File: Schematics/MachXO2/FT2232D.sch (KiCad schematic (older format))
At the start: 43 parts, among them J3 USB_B_Micro, U2 FT2232D, U4 93C56, X2 6.00MHz

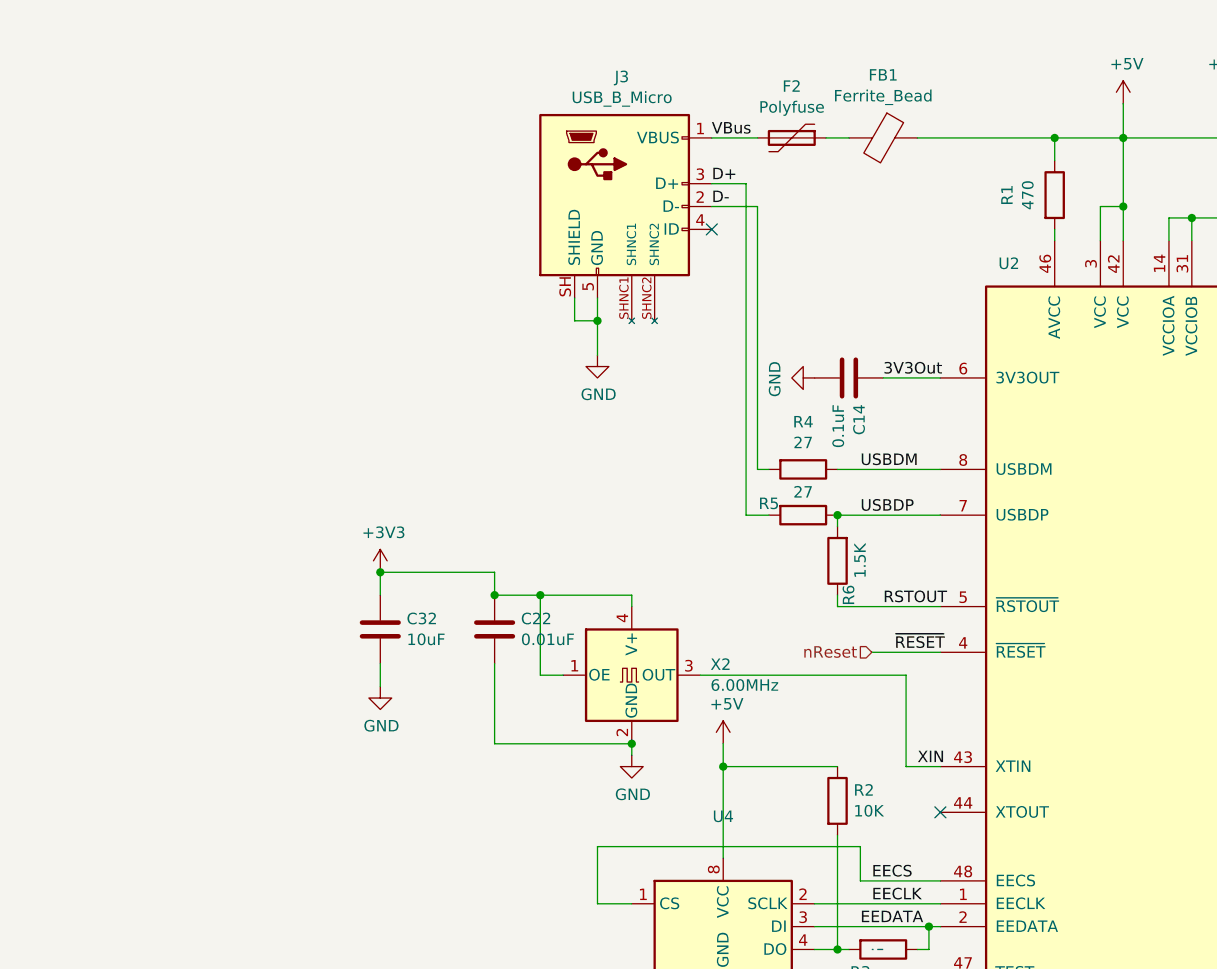
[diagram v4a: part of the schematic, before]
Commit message: asq bug fix.
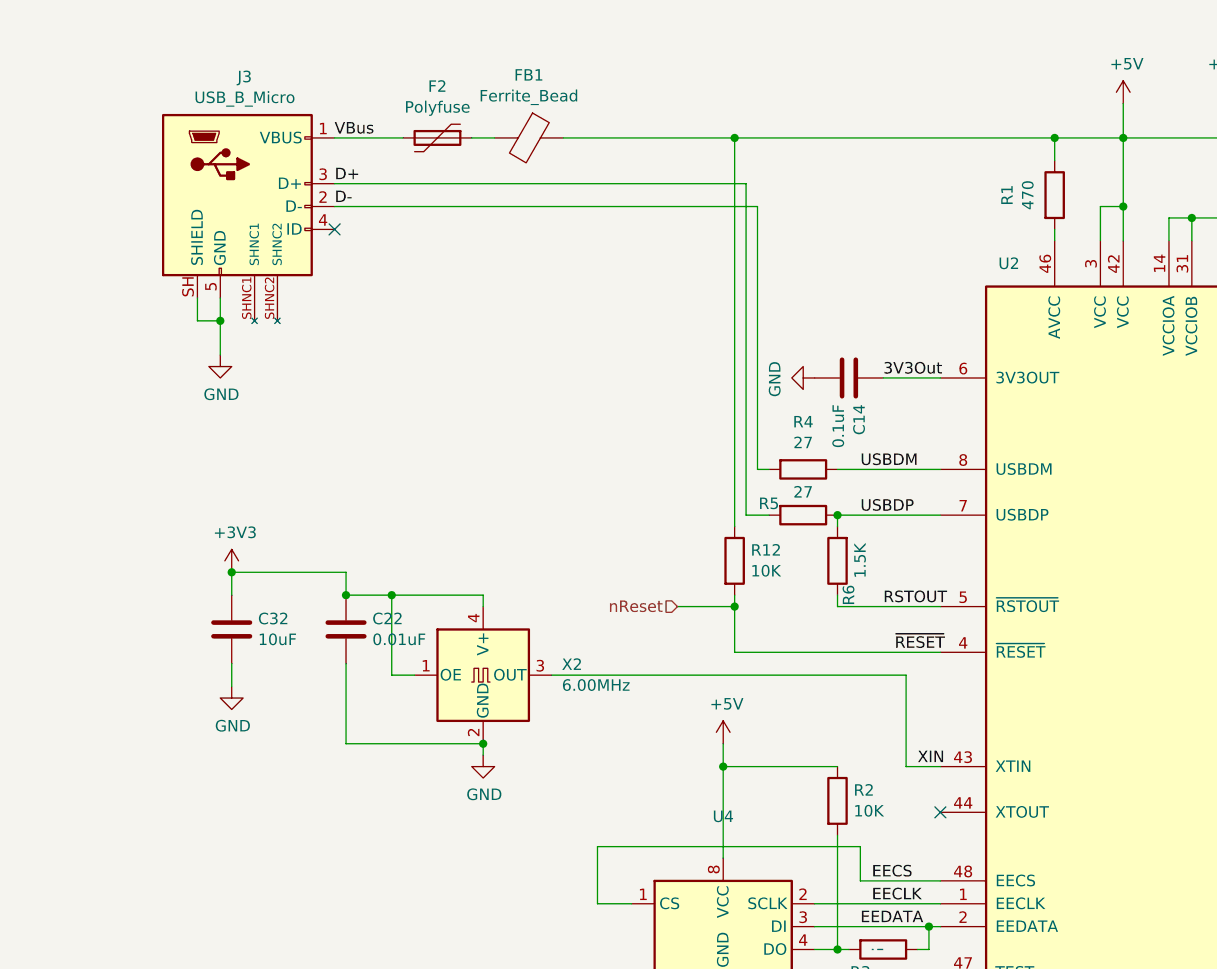
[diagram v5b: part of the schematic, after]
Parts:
- added R12: 10K, Capacitors_SMD:C_0402, symbol CPU2908CLocal:R
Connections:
- net +5V: now also R12.1
- net nReset: now also R12.2
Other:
- moved on the sheet: C22, C32, F2, FB1, J3, X2
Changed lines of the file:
@@
 L o2_breakout-rescue:USB_B_Micro-Connector J3
 U 1 1 5E6AAFE7
-P 3450 1700
+P 1800 1700
 AR Path="/5E6AAFE7" Ref="J3"  Part="1"
 AR Path="/5E6A6650/5E6AAFE7" Ref="J3"  Part="1"
-F 0 "J3" H 3507 2167 50  0000 C CNN
-F 1 "USB_B_Micro" H 3507 2076 50  0000 C CNN
-F 2 "digikey-footprints:HRS_ZX62R-B-5P" H 3600 1650 50  0001 C CNN
-F 3 "~" H 3600 1650 50  0001 C CNN
-	1    3450 1700
+F 0 "J3" H 1857 2167 50  0000 C CNN
+F 1 "USB_B_Micro" H 1857 2076 50  0000 C CNN
+F 2 "digikey-footprints:HRS_ZX62R-B-5P" H 1950 1650 50  0001 C CNN
+F 3 "~" H 1950 1650 50  0001 C CNN
+	1    1800 1700
 	1    0    0    -1
 $EndComp
@@
 L power:GND #PWR0103
 U 1 1 5DC3B558
-P 3400 2450
-F 0 "#PWR0103" H 3400 2200 50  0001 C CNN
-F 1 "GND" H 3405 2277 50  0000 C CNN
-F 2 "" H 3400 2450 50  0001 C CNN
-F 3 "" H 3400 2450 50  0001 C CNN
-	1    3400 2450
-	1    0    0    -1
-$EndComp
-NoConn ~ 3900 1900
+P 1750 2450
+F 0 "#PWR0103" H 1750 2200 50  0001 C CNN
+F 1 "GND" H 1755 2277 50  0000 C CNN
+F 2 "" H 1750 2450 50  0001 C CNN
+F 3 "" H 1750 2450 50  0001 C CNN
+	1    1750 2450
+	1    0    0    -1
+$EndComp
+NoConn ~ 2250 1900
 Wire Wire Line
 	5600 1950 5600 1800
@@
 Wire Wire Line
 	4750 5850 5500 5850
-Wire Wire Line
-	4900 3750 4600 3750
-Text HLabel 4600 3750 0    50   Input ~ 0
+Text HLabel 3750 3550 0    50   Input ~ 0
 nReset
 $Comp
@@
 L o2_breakout-rescue:SG-8002CA-Oscillator X?
 U 1 1 5DC12BA3
-P 3550 3850
+P 2900 3850
 AR Path="/5DC12BA3" Ref="X?"  Part="1"
 AR Path="/5E6A6650/5DC12BA3" Ref="X2"  Part="1"
-F 0 "X2" H 3894 3896 50  0000 L CNN
-F 1 "6.00MHz" H 3894 3805 50  0000 L CNN
-F 2 "Oscillators:Oscillator_SMD_SeikoEpson_SG8002LB-4pin_5.0x3.2mm_HandSoldering" H 4250 3500 50  0001 C CNN
-F 3 "https://support.epson.biz/td/api/doc_check.php?mode=dl&lang=en&Parts=SG-8002DC" H 3450 3850 50  0001 C CNN
-	1    3550 3850
-	1    0    0    -1
-$EndComp
-Wire Wire Line
-	3850 3850 4750 3850
+F 0 "X2" H 3244 3896 50  0000 L CNN
+F 1 "6.00MHz" H 3244 3805 50  0000 L CNN
+F 2 "Oscillators:Oscillator_SMD_SeikoEpson_SG8002LB-4pin_5.0x3.2mm_HandSoldering" H 3600 3500 50  0001 C CNN
+F 3 "https://support.epson.biz/td/api/doc_check.php?mode=dl&lang=en&Parts=SG-8002DC" H 2800 3850 50  0001 C CNN
+	1    2900 3850
+	1    0    0    -1
+$EndComp
+Wire Wire Line
+	3200 3850 4750 3850
 Wire Wire Line
 	4750 3850 4750 4250
@@
 	4750 4250 4900 4250
 Wire Wire Line
-	3550 4150 3550 4200
+	2900 4150 2900 4200
 $Comp
 L power:GND #PWR015
 U 1 1 5DC1A4C5
-P 3550 4200
-F 0 "#PWR015" H 3550 3950 50  0001 C CNN
-F 1 "GND" H 3555 4027 50  0000 C CNN
-F 2 "" H 3550 4200 50  0001 C CNN
-F 3 "" H 3550 4200 50  0001 C CNN
-	1    3550 4200
-	1    0    0    -1
-$EndComp
-Wire Wire Line
-	3250 3850 3150 3850
-Wire Wire Line
-	3150 3850 3150 3500
-Wire Wire Line
-	3150 3500 3550 3500
+P 2900 4200
+F 0 "#PWR015" H 2900 3950 50  0001 C CNN
+F 1 "GND" H 2905 4027 50  0000 C CNN
+F 2 "" H 2900 4200 50  0001 C CNN
+F 3 "" H 2900 4200 50  0001 C CNN
+	1    2900 4200
+	1    0    0    -1
+$EndComp
+Wire Wire Line
+	2600 3850 2500 3850
+Wire Wire Line
+	2500 3850 2500 3500
+Wire Wire Line
+	2500 3500 2900 3500
 Wire Wire Line
 	4450 3150 4900 3150
@@
 L o2_breakout-rescue:Ferrite_Bead-Device FB1
 U 1 1 5DC565F5
-P 4650 1500
-F 0 "FB1" V 4376 1500 50  0000 C CNN
-F 1 "Ferrite_Bead" V 4467 1500 50  0000 C CNN
-F 2 "Capacitors_SMD:C_0805" V 4580 1500 50  0001 C CNN
-F 3 "~" H 4650 1500 50  0001 C CNN
-	1    4650 1500
+P 3100 1500
+F 0 "FB1" V 2826 1500 50  0000 C CNN
+F 1 "Ferrite_Bead" V 2917 1500 50  0000 C CNN
+F 2 "Capacitors_SMD:C_0805" V 3030 1500 50  0001 C CNN
+F 3 "~" H 3100 1500 50  0001 C CNN
+	1    3100 1500
 	0    1    1    0
 $EndComp
@@
 L power:GND #PWR0112
 U 1 1 5DDF2AA2
-P 2450 3900
-F 0 "#PWR0112" H 2450 3650 50  0001 C CNN
-F 1 "GND" H 2455 3727 50  0000 C CNN
-F 2 "" H 2450 3900 50  0001 C CNN
-F 3 "" H 2450 3900 50  0001 C CNN
-	1    2450 3900
-	1    0    0    -1
-$EndComp
-Wire Wire Line
-	3550 3500 3550 3550
+P 1800 3900
+F 0 "#PWR0112" H 1800 3650 50  0001 C CNN
+F 1 "GND" H 1805 3727 50  0000 C CNN
+F 2 "" H 1800 3900 50  0001 C CNN
+F 3 "" H 1800 3900 50  0001 C CNN
+	1    1800 3900
+	1    0    0    -1
+$EndComp
+Wire Wire Line
+	2900 3500 2900 3550
 $Comp
 L Device:C C22
 U 1 1 5DECDE29
-P 2950 3650
-F 0 "C22" H 3065 3696 50  0000 L CNN
-F 1 "0.01uF" H 3065 3605 50  0000 L CNN
-F 2 "Capacitors_SMD:C_0402" H 2988 3500 50  0001 C CNN
-F 3 "~" H 2950 3650 50  0001 C CNN
-	1    2950 3650
+P 2300 3650
+F 0 "C22" H 2415 3696 50  0000 L CNN
+F 1 "0.01uF" H 2415 3605 50  0000 L CNN
+F 2 "Capacitors_SMD:C_0402" H 2338 3500 50  0001 C CNN
+F 3 "~" H 2300 3650 50  0001 C CNN
+	1    2300 3650
 	1    0    0    -1
 $EndComp
@@
 	0    1    1    0
 $EndComp
-Wire Wire Line
-	4650 2550 4900 2550
 Text Label 4650 2550 0    50   ~ 0
 3V3Out
@@
 	8300 2050 8900 2050
 Connection ~ 8300 2050
-Text Label 3900 1500 0    50   ~ 0
+Text Label 2250 1500 0    50   ~ 0
 VBus
 $Comp
 L Device:Polyfuse F?
 U 1 1 5F0067B9
-P 4250 1500
+P 2700 1500
 AR Path="/5DD58257/5F0067B9" Ref="F?"  Part="1"
 AR Path="/5E6A6650/5F0067B9" Ref="F2"  Part="1"
-F 0 "F2" V 4025 1500 50  0000 C CNN
-F 1 "Polyfuse" V 4116 1500 50  0000 C CNN
-F 2 "Capacitors_SMD:C_0805" H 4300 1300 50  0001 L CNN
-F 3 "~" H 4250 1500 50  0001 C CNN
-	1    4250 1500
+F 0 "F2" V 2475 1500 50  0000 C CNN
+F 1 "Polyfuse" V 2566 1500 50  0000 C CNN
+F 2 "Capacitors_SMD:C_0805" H 2750 1300 50  0001 L CNN
+F 3 "~" H 2700 1500 50  0001 C CNN
+	1    2700 1500
 	0    1    1    0
 $EndComp
 Connection ~ 5400 1500
 Wire Wire Line
-	4800 1500 5400 1500
-Wire Wire Line
-	4400 1500 4500 1500
+	2850 1500 2950 1500
 Wire Wire Line
 	4450 3200 4450 3150
@@
 Text Label 4550 4950 0    50   ~ 0
 EEDATA
-Text Label 3900 1700 0    50   ~ 0
+Text Label 2250 1700 0    50   ~ 0
 D+
-Text Label 3900 1800 0    50   ~ 0
+Text Label 2250 1800 0    50   ~ 0
 D-
 $Comp
@@
 $EndComp
 Wire Wire Line
-	2950 3500 3150 3500
-Connection ~ 3150 3500
-Wire Wire Line
-	2950 3800 2950 4150
-Wire Wire Line
-	2950 4150 3550 4150
-Connection ~ 3550 4150
+	2300 3500 2500 3500
+Connection ~ 2500 3500
+Wire Wire Line
+	2300 3800 2300 4150
+Wire Wire Line
+	2300 4150 2900 4150
+Connection ~ 2900 4150
 Wire Wire Line
 	3950 5250 3950 5350
@@
 	3950 4250 3950 4650
 Wire Wire Line
-	3400 2200 3400 2300
-Wire Wire Line
-	3400 2300 3300 2300
-Wire Wire Line
-	3300 2300 3300 2200
-Connection ~ 3400 2300
-Wire Wire Line
-	3400 2300 3400 2450
-Wire Wire Line
-	3900 1800 4100 1800
-Wire Wire Line
-	3900 1700 4050 1700
-Wire Wire Line
-	3900 1500 4100 1500
+	1750 2200 1750 2300
+Wire Wire Line
+	1750 2300 1650 2300
+Wire Wire Line
+	1650 2300 1650 2200
+Connection ~ 1750 2300
+Wire Wire Line
+	1750 2300 1750 2450
+Wire Wire Line
+	2250 1800 4100 1800
+Wire Wire Line
+	2250 1700 4050 1700
+Wire Wire Line
+	2250 1500 2550 1500
 $Comp
 L Device:C C32
 U 1 1 5F5AF340
-P 2450 3650
-F 0 "C32" H 2565 3696 50  0000 L CNN
-F 1 "10uF" H 2565 3605 50  0000 L CNN
-F 2 "Capacitors_SMD:C_0805_HandSoldering" H 2488 3500 50  0001 C CNN
-F 3 "~" H 2450 3650 50  0001 C CNN
-	1    2450 3650
+P 1800 3650
+F 0 "C32" H 1915 3696 50  0000 L CNN
+F 1 "10uF" H 1915 3605 50  0000 L CNN
+F 2 "Capacitors_SMD:C_0805_HandSoldering" H 1838 3500 50  0001 C CNN
+F 3 "~" H 1800 3650 50  0001 C CNN
+	1    1800 3650
 	1    0    0    -1
 $EndComp
@@
 L power:+3V3 #PWR0111
 U 1 1 5E094554
-P 2450 3400
-F 0 "#PWR0111" H 2450 3250 50  0001 C CNN
-F 1 "+3V3" H 2465 3573 50  0000 C CNN
-F 2 "" H 2450 3400 50  0001 C CNN
-F 3 "" H 2450 3400 50  0001 C CNN
-	1    2450 3400
-	1    0    0    -1
-$EndComp
-Wire Wire Line
-	2450 3400 2450 3500
-Wire Wire Line
-	2450 3800 2450 3900
-Wire Wire Line
-	2450 3400 2950 3400
-Connection ~ 2450 3400
-Connection ~ 2950 3500
-Wire Wire Line
-	2950 3400 2950 3500
+P 1800 3400
+F 0 "#PWR0111" H 1800 3250 50  0001 C CNN
+F 1 "+3V3" H 1815 3573 50  0000 C CNN
+F 2 "" H 1800 3400 50  0001 C CNN
+F 3 "" H 1800 3400 50  0001 C CNN
+	1    1800 3400
+	1    0    0    -1
+$EndComp
+Wire Wire Line
+	1800 3400 1800 3500
+Wire Wire Line
+	1800 3800 1800 3900
+Wire Wire Line
+	1800 3400 2300 3400
+Connection ~ 1800 3400
+Connection ~ 2300 3500
+Wire Wire Line
+	2300 3400 2300 3500
 Wire Wire Line
 	3100 7000 3550 7000
@@
 Text Label 6850 5050 0    50   ~ 0
 ~TxLED
+$Comp
+L CPU2908CLocal:R R12
+U 1 1 5EE304E8
+P 4000 3350
+AR Path="/5E6A6650/5EE304E8" Ref="R12"  Part="1"
+AR Path="/5EE304E8" Ref="R?"  Part="1"
+F 0 "R12" H 4070 3396 50  0000 L CNN
+F 1 "10K" H 4070 3305 50  0000 L CNN
+F 2 "Capacitors_SMD:C_0402" V 3930 3350 50  0001 C CNN
+F 3 "~" H 4000 3350 50  0001 C CNN
+	1    4000 3350
+	1    0    0    -1
+$EndComp
+Wire Wire Line
+	4650 2550 4900 2550
+Wire Wire Line
+	4000 3500 4000 3550
+Wire Wire Line
+	3750 3550 4000 3550
+Connection ~ 4000 3550
+Wire Wire Line
+	4000 3550 4000 3750
+Wire Wire Line
+	4000 3750 4900 3750
+Wire Wire Line
+	3250 1500 4000 1500
+Connection ~ 4000 1500
+Wire Wire Line
+	4000 1500 4000 3200
+Wire Wire Line
+	4000 1500 5400 1500
 $EndSCHEMATC

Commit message: PCB RevA3.
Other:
- moved on the sheet: C13
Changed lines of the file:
@@
 Connection ~ 6300 6950
 Wire Wire Line
-	6300 6950 6500 6950
+	6300 6950 6550 6950
 Connection ~ 6300 7250
 Wire Wire Line
-	6300 7250 6500 7250
+	6300 7250 6550 7250
 $Comp
 L Device:C C13
 U 1 1 5DC7B966
-P 6500 7100
-F 0 "C13" H 6615 7146 50  0000 L CNN
-F 1 "0.1uF" H 6615 7055 50  0000 L CNN
-F 2 "Capacitors_SMD:C_0402" H 6538 6950 50  0001 C CNN
-F 3 "~" H 6500 7100 50  0001 C CNN
-	1    6500 7100
+P 6550 7100
+F 0 "C13" H 6665 7146 50  0000 L CNN
+F 1 "0.1uF" H 6665 7055 50  0000 L CNN
+F 2 "Capacitors_SMD:C_0402" H 6588 6950 50  0001 C CNN
+F 3 "~" H 6550 7100 50  0001 C CNN
+	1    6550 7100
 	1    0    0    -1
 $EndComp
-Connection ~ 6500 6950
-Wire Wire Line
-	6500 6950 6550 6950
-Connection ~ 6500 7250
-Wire Wire Line
-	6500 7250 6550 7250
 $Comp
 L power:+3V3 #PWR0110

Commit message: Update Gerber Data to RevA5
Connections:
- net nReset renamed ~RESET
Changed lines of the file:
@@
 Wire Wire Line
 	4750 5850 5500 5850
-Text HLabel 3750 3550 0    50   Input ~ 0
-nReset
 $Comp
 L CPU2908CLocal:R R1
@@
 	7900 1700 7700 1700
 $Comp
-L Memory_EEPROM:93CxxA U4
-U 1 1 5DC82A54
-P 3950 4950
-F 0 "U4" H 3950 5431 50  0000 C CNN
-F 1 "93C56" H 3700 4650 50  0000 C CNN
-F 2 "Housings_SOIC:SOIC-8_3.9x4.9mm_Pitch1.27mm" H 3950 4950 50  0001 C CNN
-F 3 "http://ww1.microchip.com/downloads/en/DeviceDoc/20001749K.pdf" H 3950 4950 50  0001 C CNN
-	1    3950 4950
-	1    0    0    -1
-$EndComp
-$Comp
 L power:GND #PWR0104
 U 1 1 5DC86D51
@@
 	4350 4850 4900 4850
 Wire Wire Line
-	3400 4850 3550 4850
-Wire Wire Line
 	4350 4950 4850 4950
 Wire Wire Line
@@
 	4450 4550 4450 5050
 Wire Wire Line
-	4550 4600 3400 4600
-Wire Wire Line
 	4550 4600 4550 4750
-Wire Wire Line
-	3400 4600 3400 4850
 $Comp
 L CPU2908CLocal:R R3
@@
 	4500 5050 4450 5050
 Connection ~ 4450 5050
-$Comp
-L o2_breakout-rescue:SG-8002CA-Oscillator X?
-U 1 1 5DC12BA3
-P 2900 3850
-AR Path="/5DC12BA3" Ref="X?"  Part="1"
-AR Path="/5E6A6650/5DC12BA3" Ref="X2"  Part="1"
-F 0 "X2" H 3244 3896 50  0000 L CNN
-F 1 "6.00MHz" H 3244 3805 50  0000 L CNN
-F 2 "Oscillators:Oscillator_SMD_SeikoEpson_SG8002LB-4pin_5.0x3.2mm_HandSoldering" H 3600 3500 50  0001 C CNN
-F 3 "https://support.epson.biz/td/api/doc_check.php?mode=dl&lang=en&Parts=SG-8002DC" H 2800 3850 50  0001 C CNN
-	1    2900 3850
-	1    0    0    -1
-$EndComp
-Wire Wire Line
-	3200 3850 4750 3850
 Wire Wire Line
 	4750 3850 4750 4250
@@
 	4750 4250 4900 4250
 Wire Wire Line
-	2900 4150 2900 4200
-$Comp
-L power:GND #PWR015
-U 1 1 5DC1A4C5
-P 2900 4200
-F 0 "#PWR015" H 2900 3950 50  0001 C CNN
-F 1 "GND" H 2905 4027 50  0000 C CNN
-F 2 "" H 2900 4200 50  0001 C CNN
-F 3 "" H 2900 4200 50  0001 C CNN
-	1    2900 4200
-	1    0    0    -1
-$EndComp
-Wire Wire Line
 	2600 3850 2500 3850
 Wire Wire Line
 	2500 3850 2500 3500
-Wire Wire Line
-	2500 3500 2900 3500
 Wire Wire Line
 	4450 3150 4900 3150
@@
 	1    0    0    -1
 $EndComp
-Wire Wire Line
-	2900 3500 2900 3550
 $Comp
 L Device:C C22
@@
 Wire Wire Line
 	2300 3500 2500 3500
-Connection ~ 2500 3500
 Wire Wire Line
 	2300 3800 2300 4150
-Wire Wire Line
-	2300 4150 2900 4150
-Connection ~ 2900 4150
 Wire Wire Line
 	3950 5250 3950 5350
@@
 	4650 2550 4900 2550
 Wire Wire Line
-	4000 3500 4000 3550
-Wire Wire Line
-	3750 3550 4000 3550
-Connection ~ 4000 3550
-Wire Wire Line
-	4000 3550 4000 3750
-Wire Wire Line
 	4000 3750 4900 3750
 Wire Wire Line
@@
 Wire Wire Line
 	4000 1500 5400 1500
+Wire Wire Line
+	2300 4150 2900 4150
+Wire Wire Line
+	2900 3500 2900 3550
+Connection ~ 2500 3500
+Wire Wire Line
+	2500 3500 2900 3500
+$Comp
+L power:GND #PWR015
+U 1 1 5DC1A4C5
+P 2900 4200
+F 0 "#PWR015" H 2900 3950 50  0001 C CNN
+F 1 "GND" H 2905 4027 50  0000 C CNN
+F 2 "" H 2900 4200 50  0001 C CNN
+F 3 "" H 2900 4200 50  0001 C CNN
+	1    2900 4200
+	1    0    0    -1
+$EndComp
+Wire Wire Line
+	2900 4150 2900 4200
+Wire Wire Line
+	3200 3850 4750 3850
+Connection ~ 2900 4150
+$Comp
+L o2_breakout-rescue:SG-8002CA-Oscillator X?
+U 1 1 5DC12BA3
+P 2900 3850
+AR Path="/5DC12BA3" Ref="X?"  Part="1"
+AR Path="/5E6A6650/5DC12BA3" Ref="X2"  Part="1"
+F 0 "X2" H 3244 3896 50  0000 L CNN
+F 1 "6.00MHz" H 3244 3805 50  0000 L CNN
+F 2 "Oscillators:Oscillator_SMD_SeikoEpson_SG8002LB-4pin_5.0x3.2mm_HandSoldering" H 3600 3500 50  0001 C CNN
+F 3 "https://support.epson.biz/td/api/doc_check.php?mode=dl&lang=en&Parts=SG-8002DC" H 2800 3850 50  0001 C CNN
+	1    2900 3850
+	1    0    0    -1
+$EndComp
+Wire Wire Line
+	3400 4600 3400 4850
+Wire Wire Line
+	4550 4600 3400 4600
+Wire Wire Line
+	3400 4850 3550 4850
+$Comp
+L Memory_EEPROM:93CxxA U4
+U 1 1 5DC82A54
+P 3950 4950
+F 0 "U4" H 3950 5431 50  0000 C CNN
+F 1 "93C56" H 3700 4650 50  0000 C CNN
+F 2 "Housings_SOIC:SOIC-8_3.9x4.9mm_Pitch1.27mm" H 3950 4950 50  0001 C CNN
+F 3 "http://ww1.microchip.com/downloads/en/DeviceDoc/20001749K.pdf" H 3950 4950 50  0001 C CNN
+	1    3950 4950
+	1    0    0    -1
+$EndComp
+Wire Wire Line
+	4000 3500 4000 3750
 $EndSCHEMATC
